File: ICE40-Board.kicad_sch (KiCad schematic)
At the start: 82 parts, among them SW1 SW_Push, U1 ADP1712AUJZ-3.3, U10 FT4222HQ, U11 74LS125, U12 74LS126, U2 ADP1712AUJZ-2.5, U3 ADP1712AUJZ-1.2, U4 Barrel_Jack, U5 W25X20CLSNIG, U6 USB_C_Receptacle_USB2.0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

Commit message: everything routed just IO pins remaining
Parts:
- U5, U8: footprint W25X20CLSNIG:W25X20CLSNIG -> Package_SO:SOIC-8_3.9x4.9mm_P1.27mm
- U9: footprint SIT2001BC-S2-33E-25.0:SIT2001BC-S2-33E-25.0 -> Package_TO_SOT_SMD:SOT-23-5_HandSoldering
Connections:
- net MISO_EXT is gone; now on net MISO: H3.4 (Pin_4)
- net MISO: no longer H3.3 (Pin_3)
- net MOSI_EXT: now also H3.3 (Pin_3)
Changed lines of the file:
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@@
     (effects (font (size 1.27 1.27)) (justify right bottom))
   )
-  (label "MISO" (at 179.07 113.03 0)
+  (label "MOSI_EXT" (at 179.07 113.03 0)
     (effects (font (size 1.27 1.27)) (justify left bottom))
   )
@@
     (effects (font (size 1.27 1.27)) (justify right bottom))
   )
-  (label "MISO_EXT" (at 179.07 110.49 0)
+  (label "MISO" (at 179.07 110.49 0)
     (effects (font (size 1.27 1.27)) (justify left bottom))
   )
@@
       (effects (font (size 1.524 1.524)))
     )
-    (property "Footprint" "W25X20CLSNIG:W25X20CLSNIG" (id 2) (at 229.87 211.836 0)
+    (property "Footprint" "Package_SO:SOIC-8_3.9x4.9mm_P1.27mm" (id 2) (at 229.87 211.836 0)
       (effects (font (size 1.524 1.524)) hide)
     )
@@
   (symbol (lib_id "power:GND") (at 218.44 144.78 0) (unit 1)
     (in_bom yes) (on_board yes)
-    (property "Reference" "#PWR?" (id 0) (at 218.44 151.13 0)
+    (property "Reference" "#PWR0102" (id 0) (at 218.44 151.13 0)
       (effects (font (size 1.27 1.27)) hide)
     )
@@
       (effects (font (size 1.524 1.524)))
     )
-    (property "Footprint" "W25X20CLSNIG:W25X20CLSNIG" (id 2) (at 271.78 179.324 0)
+    (property "Footprint" "Package_SO:SOIC-8_3.9x4.9mm_P1.27mm" (id 2) (at 271.78 179.324 0)
       (effects (font (size 1.524 1.524)) hide)
     )
@@
       (effects (font (size 1.524 1.524)))
     )
-    (property "Footprint" "SIT2001BC-S2-33E-25.0:SIT2001BC-S2-33E-25.0" (id 2) (at 270.51 228.854 0)
+    (property "Footprint" "Package_TO_SOT_SMD:SOT-23-5_HandSoldering" (id 2) (at 270.51 228.854 0)
       (effects (font (size 1.524 1.524)) hide)
     )
@@
   (symbol (lib_id "power:+3V3") (at 261.62 146.05 0) (unit 1)
     (in_bom yes) (on_board yes)
-    (property "Reference" "#PWR?" (id 0) (at 261.62 149.86 0)
+    (property "Reference" "#PWR0101" (id 0) (at 261.62 149.86 0)
       (effects (font (size 1.27 1.27)) hide)
     )
@@
       (reference "#PWR082") (unit 1) (value "GND") (footprint "")
     )
-    (path "/6914c59d-3754-4af1-9c34-a108c9a97289"
-      (reference "#PWR?") (unit 1) (value "GND") (footprint "")
-    )
     (path "/f3127aa8-4fa0-47de-9985-06be44bbdf06"
-      (reference "#PWR?") (unit 1) (value "+3V3") (footprint "")
+      (reference "#PWR0101") (unit 1) (value "+3V3") (footprint "")
+    )
+    (path "/6914c59d-3754-4af1-9c34-a108c9a97289"
+      (reference "#PWR0102") (unit 1) (value "GND") (footprint "")
     )
     (path "/6ee370d5-fdd1-4fb2-bb9a-7df7bde93257"
@@
     )
     (path "/7a6b9cdf-f13b-4329-9d9a-e43f6041b320"
-      (reference "U5") (unit 1) (value "W25X20CLSNIG") (footprint "W25X20CLSNIG:W25X20CLSNIG")
+      (reference "U5") (unit 1) (value "W25X20CLSNIG") (footprint "Package_SO:SOIC-8_3.9x4.9mm_P1.27mm")
     )
     (path "/0001fea5-902d-48c7-836e-fc3524aaf22c"
@@
     )
     (path "/3e440e2a-3697-4991-a194-924ce05398cf"
-      (reference "U8") (unit 1) (value "W25X20CLSNIG") (footprint "W25X20CLSNIG:W25X20CLSNIG")
+      (reference "U8") (unit 1) (value "W25X20CLSNIG") (footprint "Package_SO:SOIC-8_3.9x4.9mm_P1.27mm")
     )
     (path "/850123b0-9e72-4333-94a9-4aa70ced4899"
-      (reference "U9") (unit 1) (value "SIT2001BI-S2-33E-25.000000G") (footprint "SIT2001BC-S2-33E-25.0:SIT2001BC-S2-33E-25.0")
+      (reference "U9") (unit 1) (value "SIT2001BI-S2-33E-25.000000G") (footprint "Package_TO_SOT_SMD:SOT-23-5_HandSoldering")
     )
     (path "/486f1dc7-2867-4a76-8284-3d08b807ec71"

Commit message: No DRC errors, board fully routed
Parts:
- IO3: footprint Connector_PinHeader_2.00mm:PinHeader_2x09_P2.00mm_Vertical -> Connector_PinHeader_2.54mm:PinHeader_2x13_P2.54mm_Vertical; symbol Connector_Generic:Conn_02x09_Odd_Even -> Connector_Generic:Conn_02x13_Odd_Even
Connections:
- net +3V3: now also IO3.1 (Pin_1); no longer IO3.2 (Pin_2)
- net 13a: now also IO3.4 (Pin_4), U7.114 (IOT_171); no longer IO3.17 (Pin_17), U7.144 (IOT_222)
- net 13b: now also IO3.3 (Pin_3), U7.115 (IOT_172); no longer IO3.18 (Pin_18), U7.143 (IOT_221)
- net 14a: now also IO3.6 (Pin_6), U7.116 (IOT_173); no longer IO3.15 (Pin_15), U7.142 (IOT_220)
- net 14b: now also IO3.5 (Pin_5), U7.117 (IOT_174); no longer IO3.16 (Pin_16), U7.141 (IOT_219)
- net 15a: now also IO3.8 (Pin_8), U7.118 (IOT_177); no longer IO3.13 (Pin_13), U7.139 (IOT_217)
- net 15b: now also IO3.7 (Pin_7), U7.119 (IOT_178); no longer IO3.14 (Pin_14), U7.138 (IOT_216)
- net 16a: now also IO3.10 (Pin_10), U7.120 (IOT_179); no longer IO3.11 (Pin_11), U7.137 (IOT_215)
- net 16b: now also IO3.9 (Pin_9), U7.121 (IOT_181); no longer IO3.12 (Pin_12), U7.136 (IOT_214)
- net 17a: now also IO3.12 (Pin_12), U7.122 (IOT_190); no longer IO3.9 (Pin_9), U7.135 (IOT_213)
- net 17b: now also IO3.11 (Pin_11), U7.124 (IOT_191); no longer IO3.10 (Pin_10), U7.134 (IOT_212)
- net 18a: now also IO3.14 (Pin_14), U7.125 (IOT_192); no longer IO3.7 (Pin_7), U7.130 (IOT_206)
- net 18b: now also IO3.13 (Pin_13), U7.128 (IOT_197_GBIN1); no longer IO3.8 (Pin_8), U7.129 (IOT_198_GBIN0)
- net 19a: now also IO3.16 (Pin_16), U7.129 (IOT_198_GBIN0); no longer IO3.5 (Pin_5), U7.128 (IOT_197_GBIN1)
- net 19b: now also IO3.15 (Pin_15), U7.130 (IOT_206); no longer IO3.6 (Pin_6), U7.125 (IOT_192)
- net 20a: now also IO3.18 (Pin_18), U7.134 (IOT_212); no longer IO3.3 (Pin_3), U7.124 (IOT_191)
- net 20b: now also IO3.17 (Pin_17), U7.135 (IOT_213); no longer IO3.4 (Pin_4), U7.122 (IOT_190)
- net 21a: now also IO3.20 (Pin_20), U7.136 (IOT_214); no longer IO2.25 (Pin_25), U7.34 (IOL_25B)
- net 21b: now also IO3.19 (Pin_19), U7.137 (IOT_215); no longer IO2.26 (Pin_26), U7.33 (IOL_25A)
- net 22a: now also IO3.22 (Pin_22), U7.138 (IOT_216); no longer IO2.23 (Pin_23), U7.32 (IOL_24B)
- net 22b: now also IO3.21 (Pin_21), U7.139 (IOT_217); no longer IO2.24 (Pin_24), U7.31 (IOL_24A)
- net 23a: now also IO3.24 (Pin_24), U7.141 (IOT_219); no longer IO2.21 (Pin_21), U7.29 (IOL_23B)
- net 23b: now also IO3.23 (Pin_23), U7.142 (IOT_220); no longer IO2.22 (Pin_22), U7.28 (IOL_23A)
- net 24a: now also IO3.26 (Pin_26), U7.143 (IOT_221); no longer IO2.19 (Pin_19), U7.26 (IOL_18B)
- net 24b: now also IO3.25 (Pin_25), U7.144 (IOT_222); no longer IO2.20 (Pin_20), U7.25 (IOL_18A)
- net 25a: now also IO2.25 (Pin_25), U7.7 (IOL_4A); no longer IO2.17 (Pin_17), U7.24 (IOL_17B)
- net 25b: now also IO2.26 (Pin_26), U7.8 (IOL_4B); no longer IO2.18 (Pin_18), U7.23 (IOL_17A)
- net 26a: now also IO2.23 (Pin_23), U7.9 (IOL_5A); no longer IO2.15 (Pin_15), U7.22 (IOL_14B)
- net 26b: now also IO2.24 (Pin_24), U7.10 (IOL_5B); no longer IO2.16 (Pin_16), U7.21 (IOL_14A_GBIN6)
- net 27a: now also IO2.21 (Pin_21), U7.11 (IOL_8A); no longer IO2.13 (Pin_13), U7.20 (IOL_13B_GBIN7)
- net 27b: now also IO2.22 (Pin_22), U7.12 (IOL_8B); no longer IO2.14 (Pin_14), U7.19 (IOL_13A)
- net 28a: now also IO2.19 (Pin_19), U7.15 (IOL_10A); no longer IO2.11 (Pin_11), U7.18 (IOL_12B)
- net 28b: now also IO2.20 (Pin_20), U7.16 (IOL_10B); no longer IO2.12 (Pin_12), U7.17 (IOL_12A)
- net 29a: now also IO2.17 (Pin_17), U7.17 (IOL_12A); no longer IO2.9 (Pin_9), U7.16 (IOL_10B)
- net 29b: now also IO2.18 (Pin_18), U7.18 (IOL_12B); no longer IO2.10 (Pin_10), U7.15 (IOL_10A)
- net 30a: now also IO2.15 (Pin_15), U7.19 (IOL_13A); no longer IO2.7 (Pin_7), U7.12 (IOL_8B)
- net 30b: now also IO2.16 (Pin_16), U7.20 (IOL_13B_GBIN7); no longer IO2.8 (Pin_8), U7.11 (IOL_8A)
- net 31a: now also IO2.13 (Pin_13), U7.21 (IOL_14A_GBIN6); no longer IO2.5 (Pin_5), U7.10 (IOL_5B)
- net 31b: now also IO2.14 (Pin_14), U7.22 (IOL_14B); no longer IO2.6 (Pin_6), U7.9 (IOL_5A)
- net 32a: now also IO2.11 (Pin_11), U7.23 (IOL_17A); no longer IO2.3 (Pin_3), U7.8 (IOL_4B)
- net 32b: now also IO2.12 (Pin_12), U7.24 (IOL_17B); no longer IO2.4 (Pin_4), U7.7 (IOL_4A)
- net GND: now also IO3.2 (Pin_2); no longer IO3.1 (Pin_1)
- new net 33a: IO2.9 (Pin_9), U7.25 (IOL_18A)
- new net 33b: IO2.10 (Pin_10), U7.26 (IOL_18B)
- new net 34a: IO2.7 (Pin_7), U7.28 (IOL_23A)
- new net 34b: IO2.8 (Pin_8), U7.29 (IOL_23B)
- new net 35a: IO2.5 (Pin_5), U7.31 (IOL_24A)
- new net 35b: IO2.6 (Pin_6), U7.32 (IOL_24B)
- new net 36a: IO2.3 (Pin_3), U7.33 (IOL_25A)
- new net 36b: IO2.4 (Pin_4), U7.34 (IOL_25B)
- no-connect marks 40 -> 32

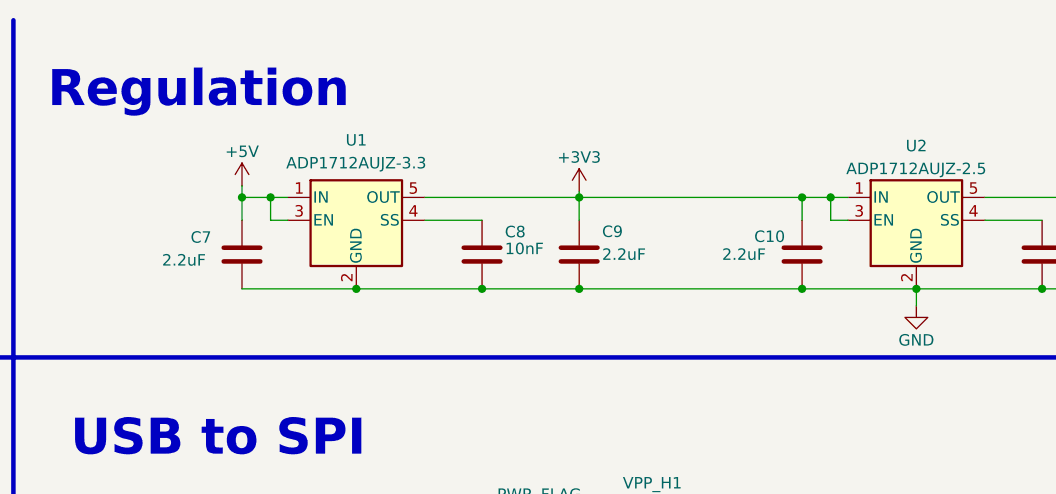
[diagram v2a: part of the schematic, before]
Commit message: Adjusted component and track clearances
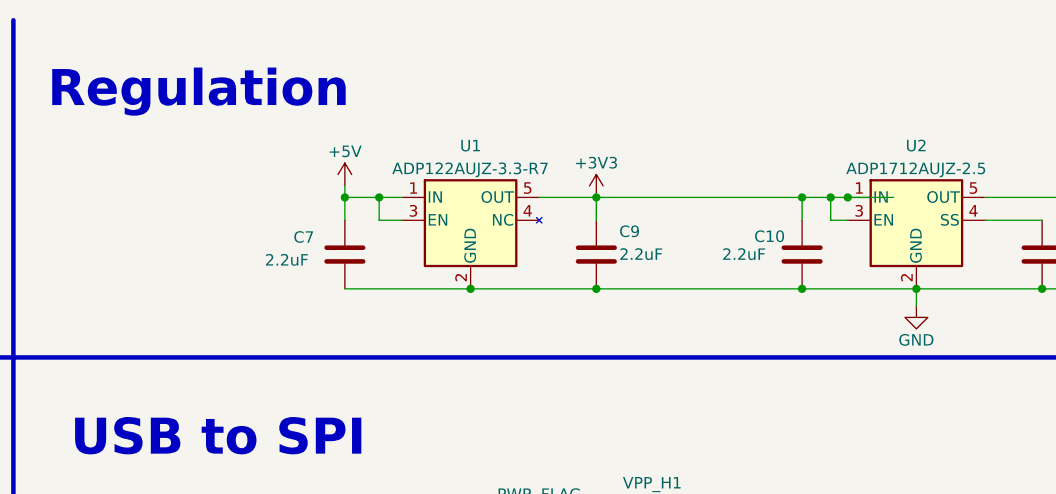
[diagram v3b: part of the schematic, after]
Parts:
- removed C8: 10nF, Capacitor_SMD:C_0603_1608Metric_Pad1.08x0.95mm_HandSolder, symbol Device:C
- U1: value ADP1712AUJZ-3.3 -> ADP122AUJZ-3.3-R7
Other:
- moved on the sheet: C7, C9

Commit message: Added ground vias for better signal integrity, added silkscreen text, added reset button for MCU
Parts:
- added R20: 10k, Resistor_SMD:R_0603_1608Metric_Pad0.98x0.95mm_HandSolder, symbol Device:R
- added SW2: SW_Push, Button_Switch_THT:SW_PUSH_6mm, symbol Switch:SW_Push
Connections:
- net +3V3: now also IO3.2 (Pin_2), R20.2; no longer IO3.1 (Pin_1)
- net GND: now also IO3.1 (Pin_1), SW2.2; no longer IO3.2 (Pin_2)
- net MCU_RESET: now reaches U7.110 (IOT_168)
- net MCU_RESET: now also R20.1, SW2.1
- no-connect marks 32 -> 31

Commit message: Placed vias around SPI lines, placed main oscillator closer to FPGA
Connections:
- net FPGA_CLK: now reaches U7.52 (IOB_82_GBIN4), U9.5 (OUT)
- net MCU_RESET: no longer names the net of R20.1, SW2.1, U7.110 (IOT_168)
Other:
- note added: "Buffers power"
- note added: "FPGA oscillator"
- note added: "MCU Reset button"
- moved on the sheet: C1, C10, C11, C12, C13, C14, C15, C16, C18, C19, C2, C20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
